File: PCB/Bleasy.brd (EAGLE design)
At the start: 30.8 x 60.3 mm, 14 parts, among them IC1 ATMEGA328-PU, Q1 8 MHz

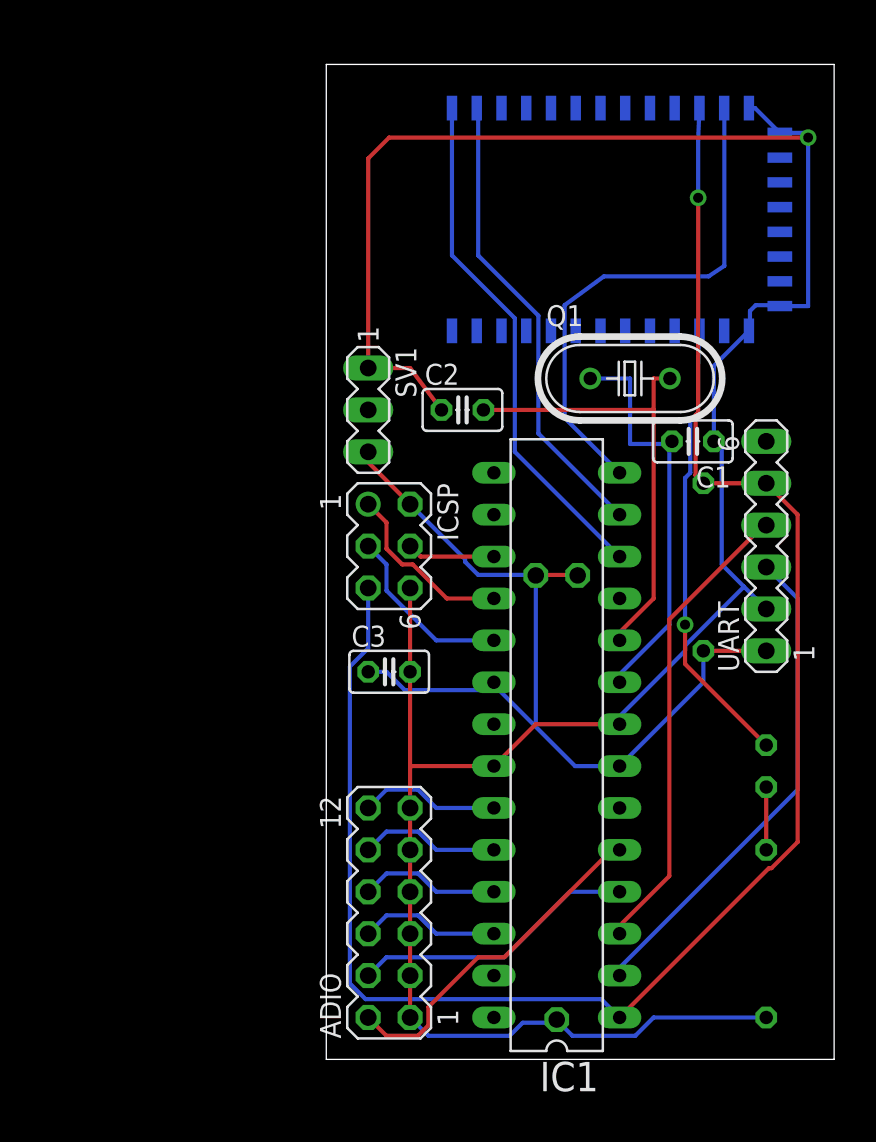
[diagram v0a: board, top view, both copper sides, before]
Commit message: board: removed via under hm10
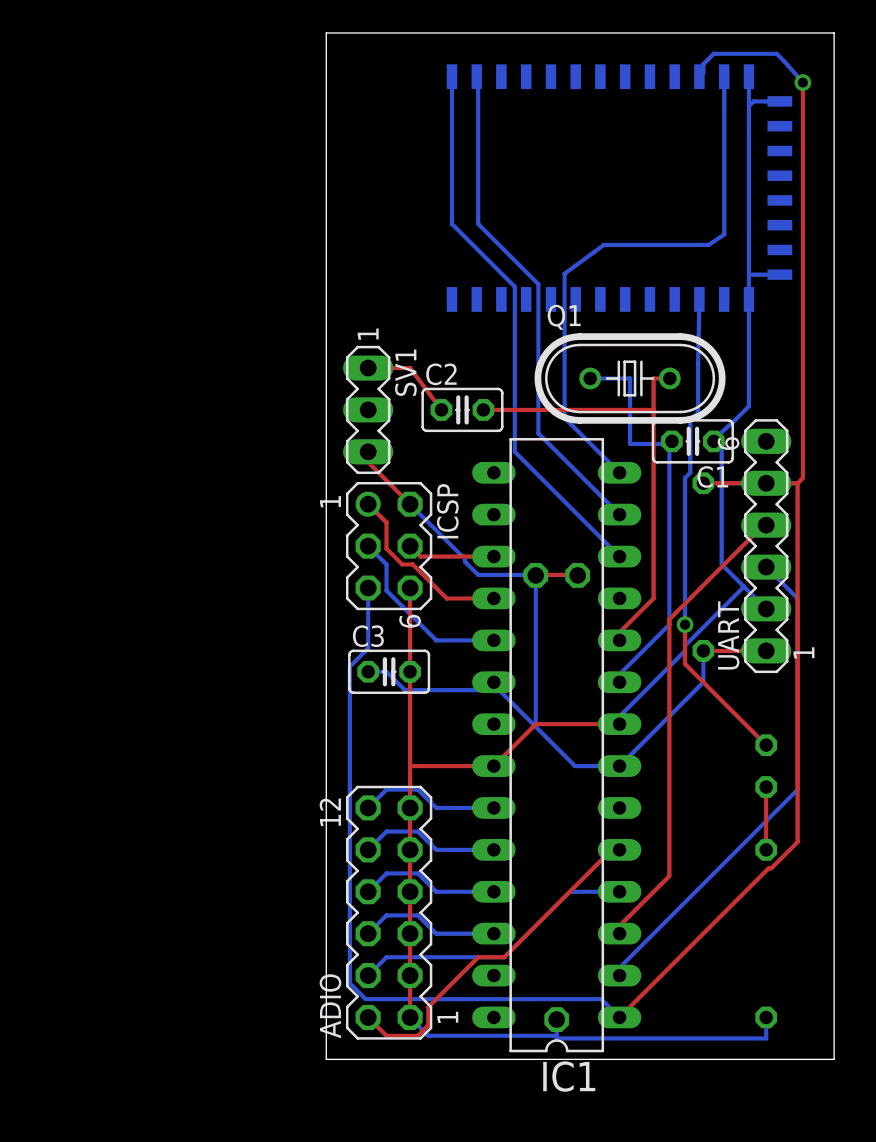
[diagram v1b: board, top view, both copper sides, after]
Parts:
- moved E1 1.91 mm to (7.62, 52.1)
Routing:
- net GND: track 159.1 -> 120.0 mm, vias 1 -> 0
- net RST: track 106.2 -> 116.6 mm
- net N$8: track 31.6 -> 33.5 mm
- net HM10_TX: track 31.4 -> 33.3 mm
- net HM10_RX: track 28.2 -> 30.1 mm
- net N$6: track 27.5 -> 29.4 mm
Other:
- board size 30.8 x 60.3 mm -> 30.8 x 62.2 mm

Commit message: minor board changes, added Text
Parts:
- moved LED1 3.17 mm to (26.7, 21.0)
- moved C2 0.32 mm to (8.57, 39.4)
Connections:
- new net N$13: E1.3, E1.4
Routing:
- net TX: track 28.5 -> 32.2 mm
- net RST: track 116.6 -> 120.1 mm
- net RX: track 30.0 -> 33.5 mm
- net N$7: track 3.81 -> 6.98 mm
- net N$8: track 33.5 -> 32.5 mm
- net N$6: track 29.4 -> 28.4 mm
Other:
- board text added: "BLEasy"
- board text added: "v.0.1, by obayer&mschaff github.com/obayer/bleazy"

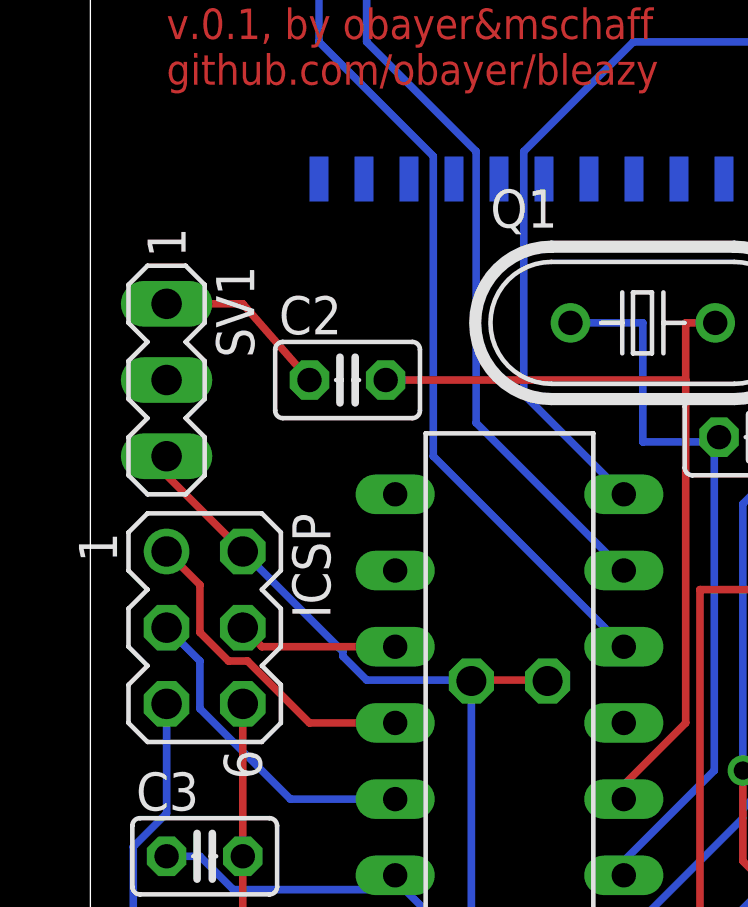
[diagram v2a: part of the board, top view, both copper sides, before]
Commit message: fix: Added missing GND line
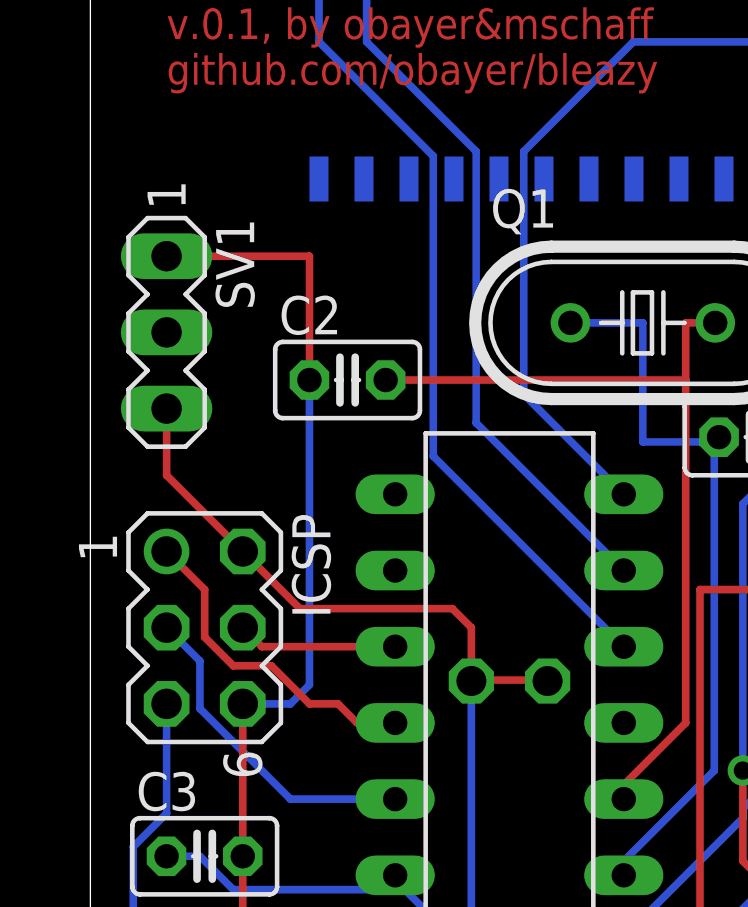
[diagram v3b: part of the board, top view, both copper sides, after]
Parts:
- moved SV1 1.59 mm to (2.54, 41.0)
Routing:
- net GND: track 119.9 -> 135.5 mm
- net +3V3: track 56.5 -> 59.0 mm
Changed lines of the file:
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@@
 <?xml version="1.0" encoding="utf-8"?>
 <!DOCTYPE eagle SYSTEM "eagle.dtd">
-<eagle version="6.5.0">
+<eagle version="7.0.0">
 <drawing>
 <settings>
@@
 <pass name="Default">
 <param name="RoutingGrid" value="6.25mil"/>
+<param name="AutoGrid" value="1"/>
+<param name="Efforts" value="0"/>
+<param name="TopRouterVariant" value="1"/>
 <param name="tpViaShape" value="round"/>
 <param name="PrefDir.1" value="*"/>
@@
 <element name="R2" library="rcl" package="0207/10" value="270" x="26.67" y="7.62" rot="MR90"/>
 <element name="LED1" library="led" package="LED3MM" value="" x="26.67" y="20.955" rot="MR270"/>
-<element name="SV1" library="con-lstb" package="MA03-1" value="" x="2.54" y="39.37" rot="R270">
-<attribute name="OC_NEWARK" value="unknown" x="2.54" y="39.37" size="1.778" layer="27" rot="R270" display="off"/>
-<attribute name="MPN" value="" x="2.54" y="39.37" size="1.778" layer="27" rot="R270" display="off"/>
-<attribute name="MF" value="" x="2.54" y="39.37" size="1.778" layer="27" rot="R270" display="off"/>
-<attribute name="OC_FARNELL" value="unknown" x="2.54" y="39.37" size="1.778" layer="27" rot="R270" display="off"/>
+<element name="SV1" library="con-lstb" package="MA03-1" value="" x="2.54" y="40.9575" rot="R270">
+<attribute name="OC_NEWARK" value="unknown" x="2.54" y="40.9575" size="1.778" layer="27" rot="R270" display="off"/>
+<attribute name="MPN" value="" x="2.54" y="40.9575" size="1.778" layer="27" rot="R270" display="off"/>
+<attribute name="MF" value="" x="2.54" y="40.9575" size="1.778" layer="27" rot="R270" display="off"/>
+<attribute name="OC_FARNELL" value="unknown" x="2.54" y="40.9575" size="1.778" layer="27" rot="R270" display="off"/>
 </element>
 <element name="ADIO" library="con-lstb" package="MA06-2" value="" x="3.81" y="8.89" rot="R90">
@@
 <wire x1="25.62" y1="39.59" x2="25.62" y2="46.07" width="0.254" layer="16"/>
 <wire x1="27.44" y1="47.625" x2="27.495" y2="47.57" width="0.254" layer="16"/>
-<wire x1="2.54" y1="41.91" x2="5.08" y2="41.91" width="0.254" layer="1"/>
-<wire x1="5.08" y1="41.91" x2="7.3025" y2="39.37" width="0.254" layer="1"/>
+<wire x1="2.54" y1="43.4975" x2="7.3025" y2="43.4975" width="0.254" layer="1"/>
+<wire x1="7.3025" y1="43.4975" x2="7.3025" y2="39.37" width="0.254" layer="1"/>
 <wire x1="13.97" y1="1.27" x2="13.97" y2="2.413" width="0.254" layer="16"/>
 <wire x1="26.67" y1="2.54" x2="26.67" y2="1.905" width="0.254" layer="16"/>
@@
 <wire x1="6.35" y1="1.27" x2="26.035" y2="1.27" width="0.254" layer="16"/>
 <wire x1="26.035" y1="1.27" x2="26.67" y2="1.905" width="0.254" layer="16"/>
-<wire x1="5.08" y1="28.575" x2="7.3025" y2="39.37" width="0" layer="19" extent="1-1"/>
 <wire x1="13.97" y1="1.27" x2="6.35" y2="1.27" width="0" layer="19" extent="16-16"/>
+<wire x1="7.3025" y1="39.37" x2="7.3025" y2="29.21" width="0.254" layer="16"/>
+<wire x1="7.3025" y1="29.21" x2="6.6675" y2="28.575" width="0.254" layer="16"/>
+<wire x1="6.6675" y1="28.575" x2="5.08" y2="28.575" width="0.254" layer="16"/>
 </signal>
 <signal name="+3V3">
@@
 <contactref element="BAT2" pad="3"/>
 <contactref element="BAT2" pad="2"/>
-<wire x1="2.54" y1="36.195" x2="2.54" y2="36.83" width="0.254" layer="1"/>
+<wire x1="2.54" y1="36.195" x2="2.54" y2="38.4175" width="0.254" layer="1"/>
 <wire x1="5.08" y1="33.655" x2="2.54" y2="36.195" width="0.254" layer="1"/>
 <wire x1="26.67" y1="24.765" x2="22.86" y2="24.765" width="0.254" layer="1"/>
@@
 <wire x1="22.86" y1="22.86" x2="22.86" y2="24.765" width="0.254" layer="16"/>
 <wire x1="17.78" y1="17.78" x2="22.86" y2="22.86" width="0.254" layer="16"/>
-<wire x1="8.41375" y1="30.32125" x2="5.08" y2="33.655" width="0.254" layer="16"/>
-<wire x1="8.41375" y1="30.1625" x2="8.41375" y2="30.32125" width="0.254" layer="16"/>
-<wire x1="9.2075" y1="29.36875" x2="8.41375" y2="30.1625" width="0.254" layer="16"/>
-<wire x1="12.7" y1="29.36875" x2="9.2075" y2="29.36875" width="0.254" layer="16"/>
-<wire x1="12.7" y1="29.36875" x2="12.7" y2="29.337" width="0.254" layer="16"/>
+<wire x1="12.7" y1="29.36875" x2="12.7" y2="31.115" width="0.254" layer="1"/>
+<wire x1="12.7" y1="31.115" x2="12.065" y2="31.75" width="0.254" layer="1"/>
+<wire x1="12.065" y1="31.75" x2="6.985" y2="31.75" width="0.254" layer="1"/>
+<wire x1="6.985" y1="31.75" x2="5.08" y2="33.655" width="0.254" layer="1"/>
 </signal>
 <signal name="RST">
@@
 <contactref element="IC1" pad="18"/>
 <contactref element="ICSP" pad="1"/>
-<wire x1="7.3025" y1="27.94" x2="10.16" y2="27.94" width="0.254" layer="1"/>
-<wire x1="5.23875" y1="30.00375" x2="7.3025" y2="27.94" width="0.254" layer="1"/>
-<wire x1="4.60375" y1="30.00375" x2="5.23875" y2="30.00375" width="0.254" layer="1"/>
-<wire x1="3.65125" y1="30.95625" x2="4.60375" y2="30.00375" width="0.254" layer="1"/>
-<wire x1="3.65125" y1="32.54375" x2="3.65125" y2="30.95625" width="0.254" layer="1"/>
-<wire x1="2.54" y1="33.655" x2="3.65125" y2="32.54375" width="0.254" layer="1"/>
+<wire x1="10.16" y1="27.94" x2="8.89" y2="27.94" width="0.254" layer="1"/>
+<wire x1="8.89" y1="27.94" x2="8.255" y2="28.575" width="0.254" layer="1"/>
+<wire x1="8.255" y1="28.575" x2="7.3025" y2="28.575" width="0.254" layer="1"/>
+<wire x1="7.3025" y1="28.575" x2="6.0325" y2="29.845" width="0.254" layer="1"/>
+<wire x1="6.0325" y1="29.845" x2="4.7625" y2="29.845" width="0.254" layer="1"/>
+<wire x1="4.7625" y1="29.845" x2="3.81" y2="30.7975" width="0.254" layer="1"/>
+<wire x1="3.81" y1="30.7975" x2="3.81" y2="32.385" width="0.254" layer="1"/>
+<wire x1="3.81" y1="32.385" x2="2.54" y2="33.655" width="0.254" layer="1"/>
 </signal>
 <signal name="SCK">

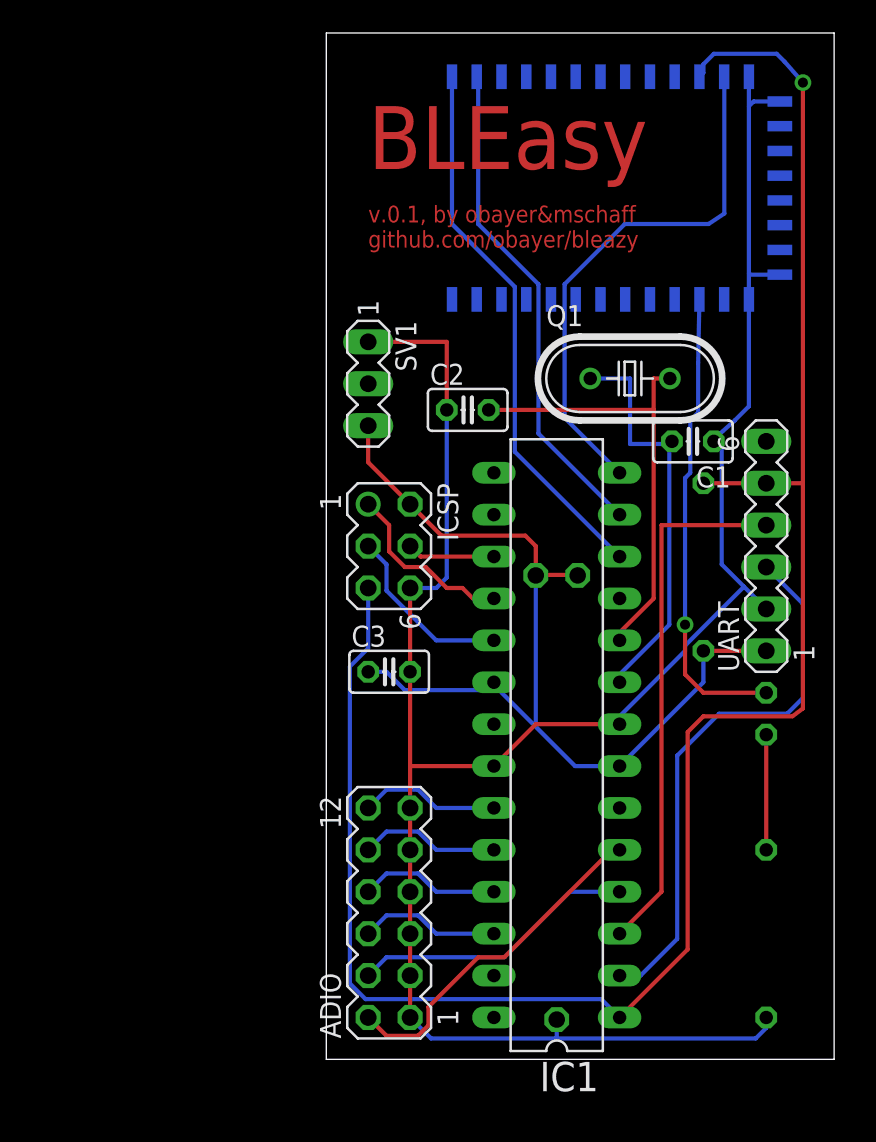
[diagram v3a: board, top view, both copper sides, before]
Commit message: reordered Pingheaders, SMD
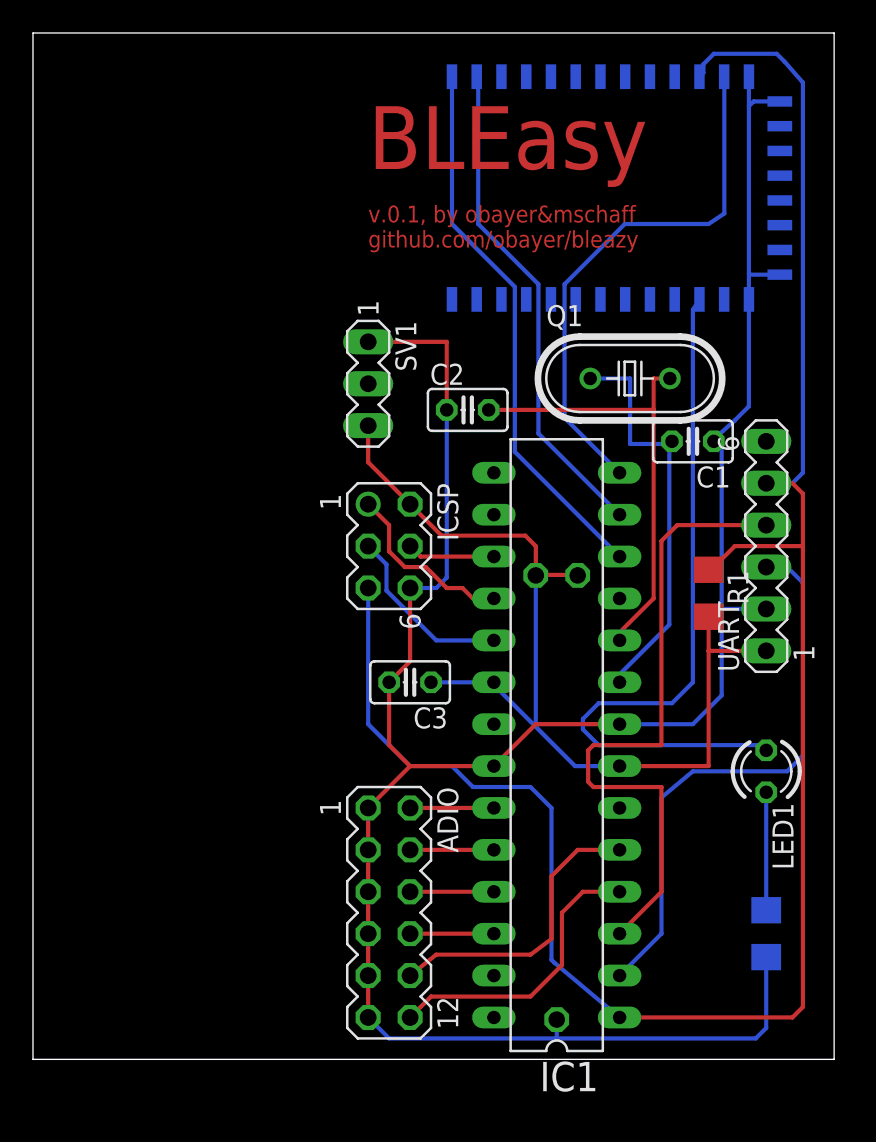
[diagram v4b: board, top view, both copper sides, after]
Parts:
- R1, R2: device rcl:0207/10 -> resistor:R1206
- moved LED1 3.49 mm to (26.7, 17.5), flipped to the top
- moved R1 1.62 mm to (23.2, 28.3), flipped to the top
- moved C3 1.42 mm to (5.08, 22.9), turned to 180 degrees
- turned ADIO to 270 degrees
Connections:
- net N$10: now also ADIO.4; no longer ADIO.10
- net N$11: now also ADIO.6; no longer ADIO.8
- net N$12: now also ADIO.8; no longer ADIO.6
- net N$4: now also ADIO.12, IC1.4; no longer ADIO.2, IC1.5
- net N$5: now also ADIO.10, IC1.5; no longer ADIO.4, IC1.4
- net N$9: now also ADIO.2; no longer ADIO.12
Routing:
- net N$6: track 28.4 -> 43.2 mm, vias 1 -> 0
- net GND: track 135.5 -> 146.1 mm
- net TX: track 32.2 -> 40.1 mm
- net N$9: track 8.54 -> 5.08 mm
- net N$11: track 8.54 -> 5.08 mm
- net N$10: track 8.54 -> 5.08 mm
- net N$12: track 8.54 -> 5.08 mm
- net N$4: track 21.0 -> 17.7 mm
- net RST: track 120.1 -> 121.4 mm, vias 1 -> 0
- net RX: track 33.5 -> 34.5 mm
- net N$5: track 17.3 -> 17.9 mm
- net +3V3: track 59.0 -> 59.5 mm
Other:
- board size 30.8 x 62.2 mm -> 48.6 x 62.2 mm

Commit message: added ground plane
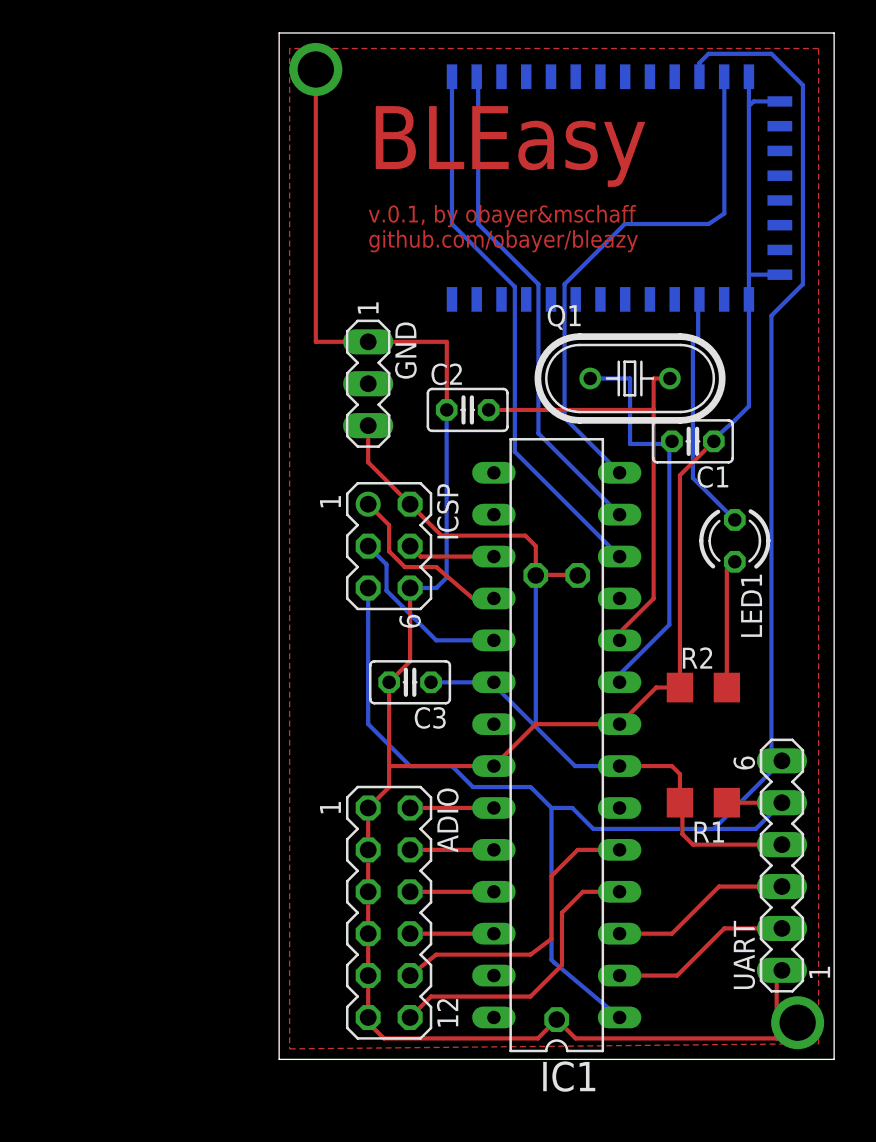
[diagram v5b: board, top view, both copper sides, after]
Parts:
- moved UART 19.4 mm to (27.6, 11.7)
- moved R2 15.4 mm to (22.9, 22.5), flipped to the top, turned to 0 degrees
- moved LED1 14.1 mm to (24.8, 31.4)
- moved R1 12.7 mm to (22.9, 15.6), turned to 180 degrees
- renumbered SV1 to GND
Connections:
- net +3V3: now also UART.4; no longer UART.1
- net GND: now also UART.1; no longer UART.2
- net RX: now also UART.2; no longer UART.3
- net TX: now also UART.3; no longer UART.4
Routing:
- net TX: track 40.1 -> 11.0 mm
- net N$6: track 43.2 -> 14.6 mm
- net RX: track 34.5 -> 11.0 mm
- net GND: track 146.1 -> 163.0 mm, vias 0 -> 2
- net RST: track 121.4 -> 110.0 mm
- net +3V3: track 59.5 -> 55.4 mm
- net N$7: track 7.15 -> 7.82 mm
- added copper zone on layer 1, net GND
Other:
- board size 48.6 x 62.2 mm -> 33.6 x 62.2 mm
